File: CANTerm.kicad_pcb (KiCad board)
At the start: 2 copper layers, 23.8 x 20 mm, 12 parts, among them J1 DB9_Male, J2 DB9_Female

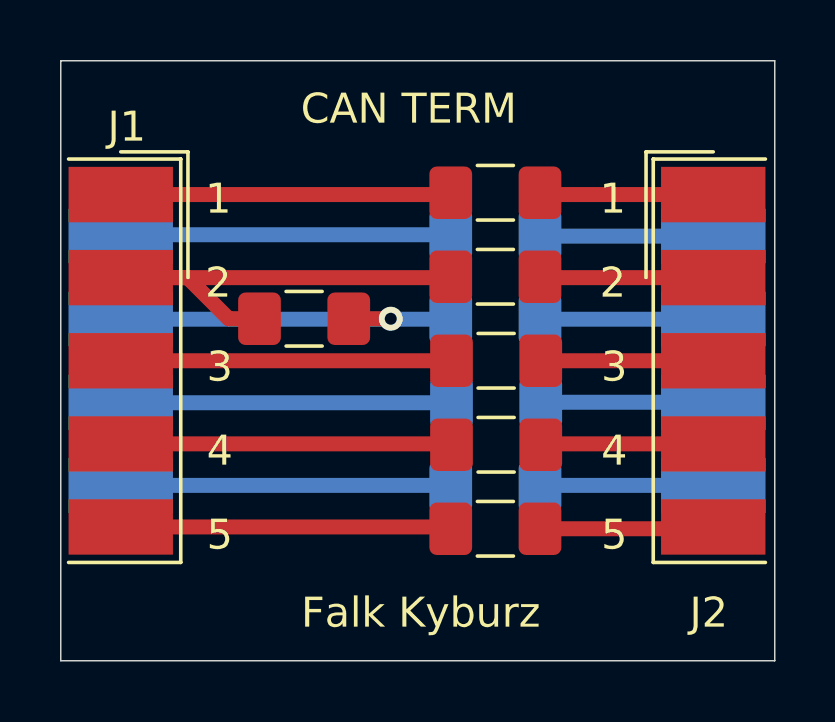
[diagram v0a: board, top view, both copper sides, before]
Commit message: Updated silk screen and added traces to bridge jumpers with solder.
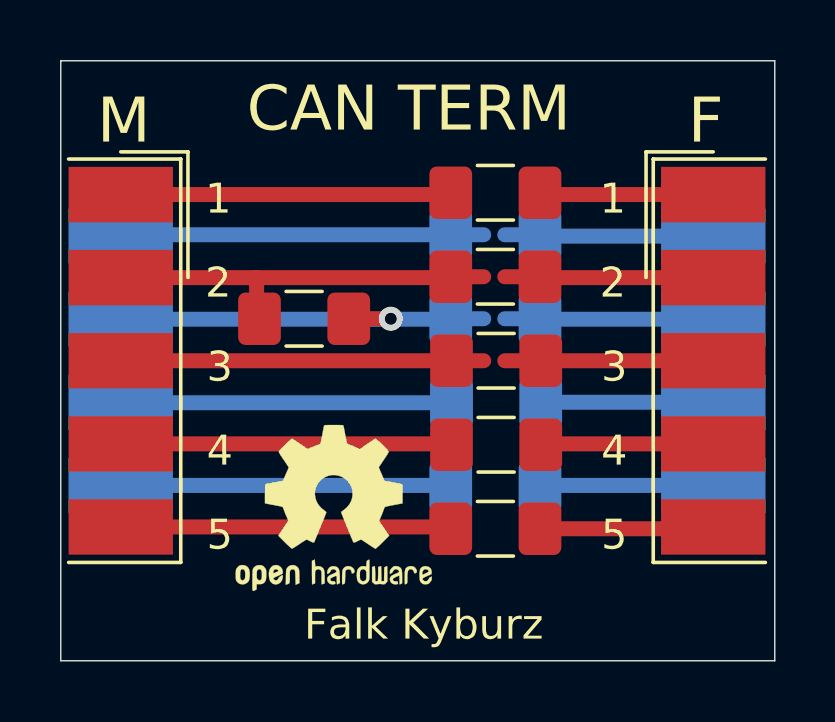
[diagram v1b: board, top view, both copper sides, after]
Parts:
- added REF**: OSHW-Logo2_7.3x6mm_SilkScreen, Symbol:OSHW-Logo2_7.3x6mm_SilkScreen, F.Cu at (165.9, 102.9)
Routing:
- net /CAN_L: track 16.2 -> 13.5 mm
- net Net-(J2-Pad3): track 5.75 -> 6.95 mm
- net Net-(J2-Pad7): track 5.78 -> 6.96 mm
- net Net-(J2-Pad6): track 5.79 -> 6.97 mm
- net Net-(J2-Pad2): track 5.79 -> 6.96 mm
- net /GND_0: track 11.0 -> 12.1 mm
- net /CAN_H: track 12.4 -> 13.5 mm
- net /GND_1: track 11.0 -> 12.1 mm
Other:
- board text added: "F"
- board text added: "M"
- board text added: "github.com/falkkyburz/canterm"
